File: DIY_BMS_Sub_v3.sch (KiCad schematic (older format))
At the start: 35 parts, among them J1 Conn_01x11, J2 Conn_02x04_Top_Bottom, J3 Conn_02x03_Top_Bottom, J4 Conn_02x03_Top_Bottom, SW1 SW_DIP_x04, U1 BQ76PL536A

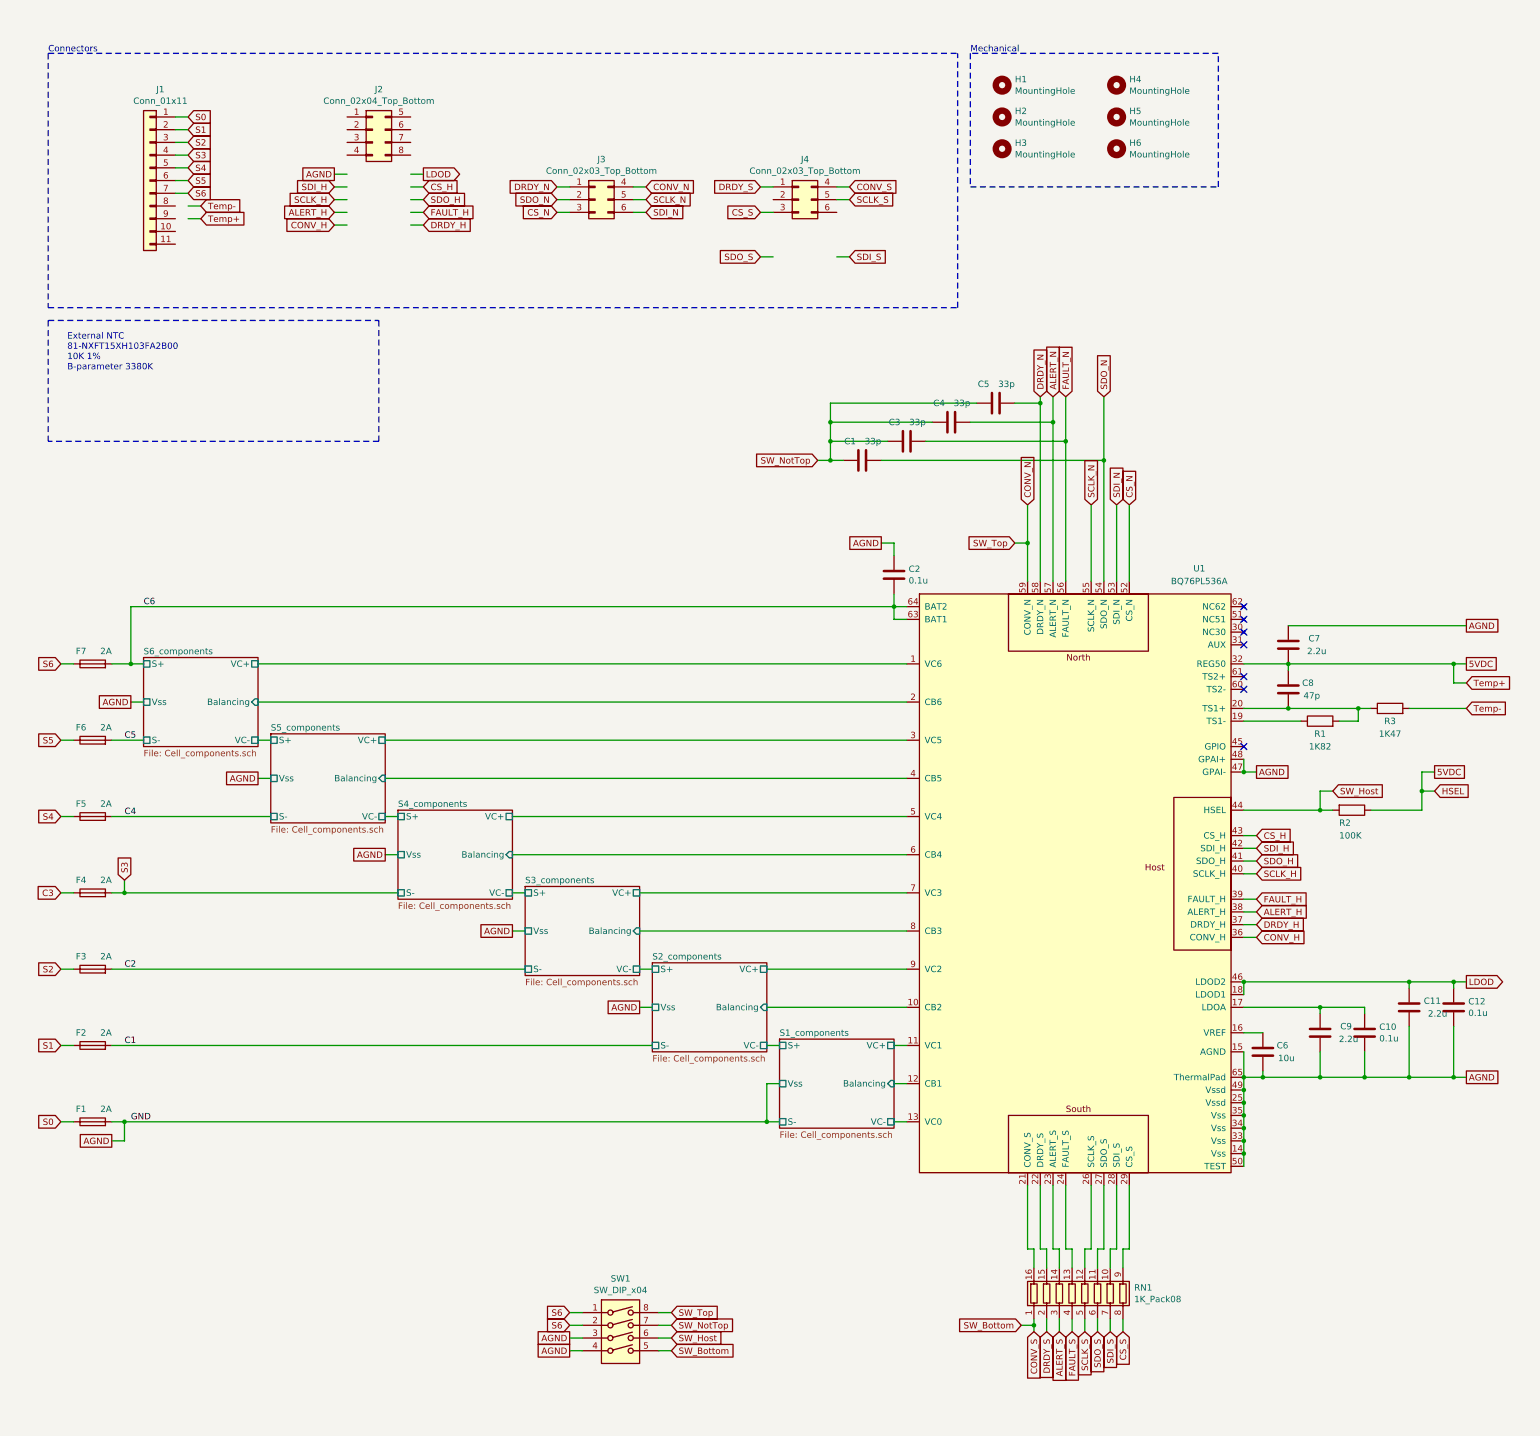
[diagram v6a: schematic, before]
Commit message: Add files via upload
Placed most components. Started routing and placing vias.
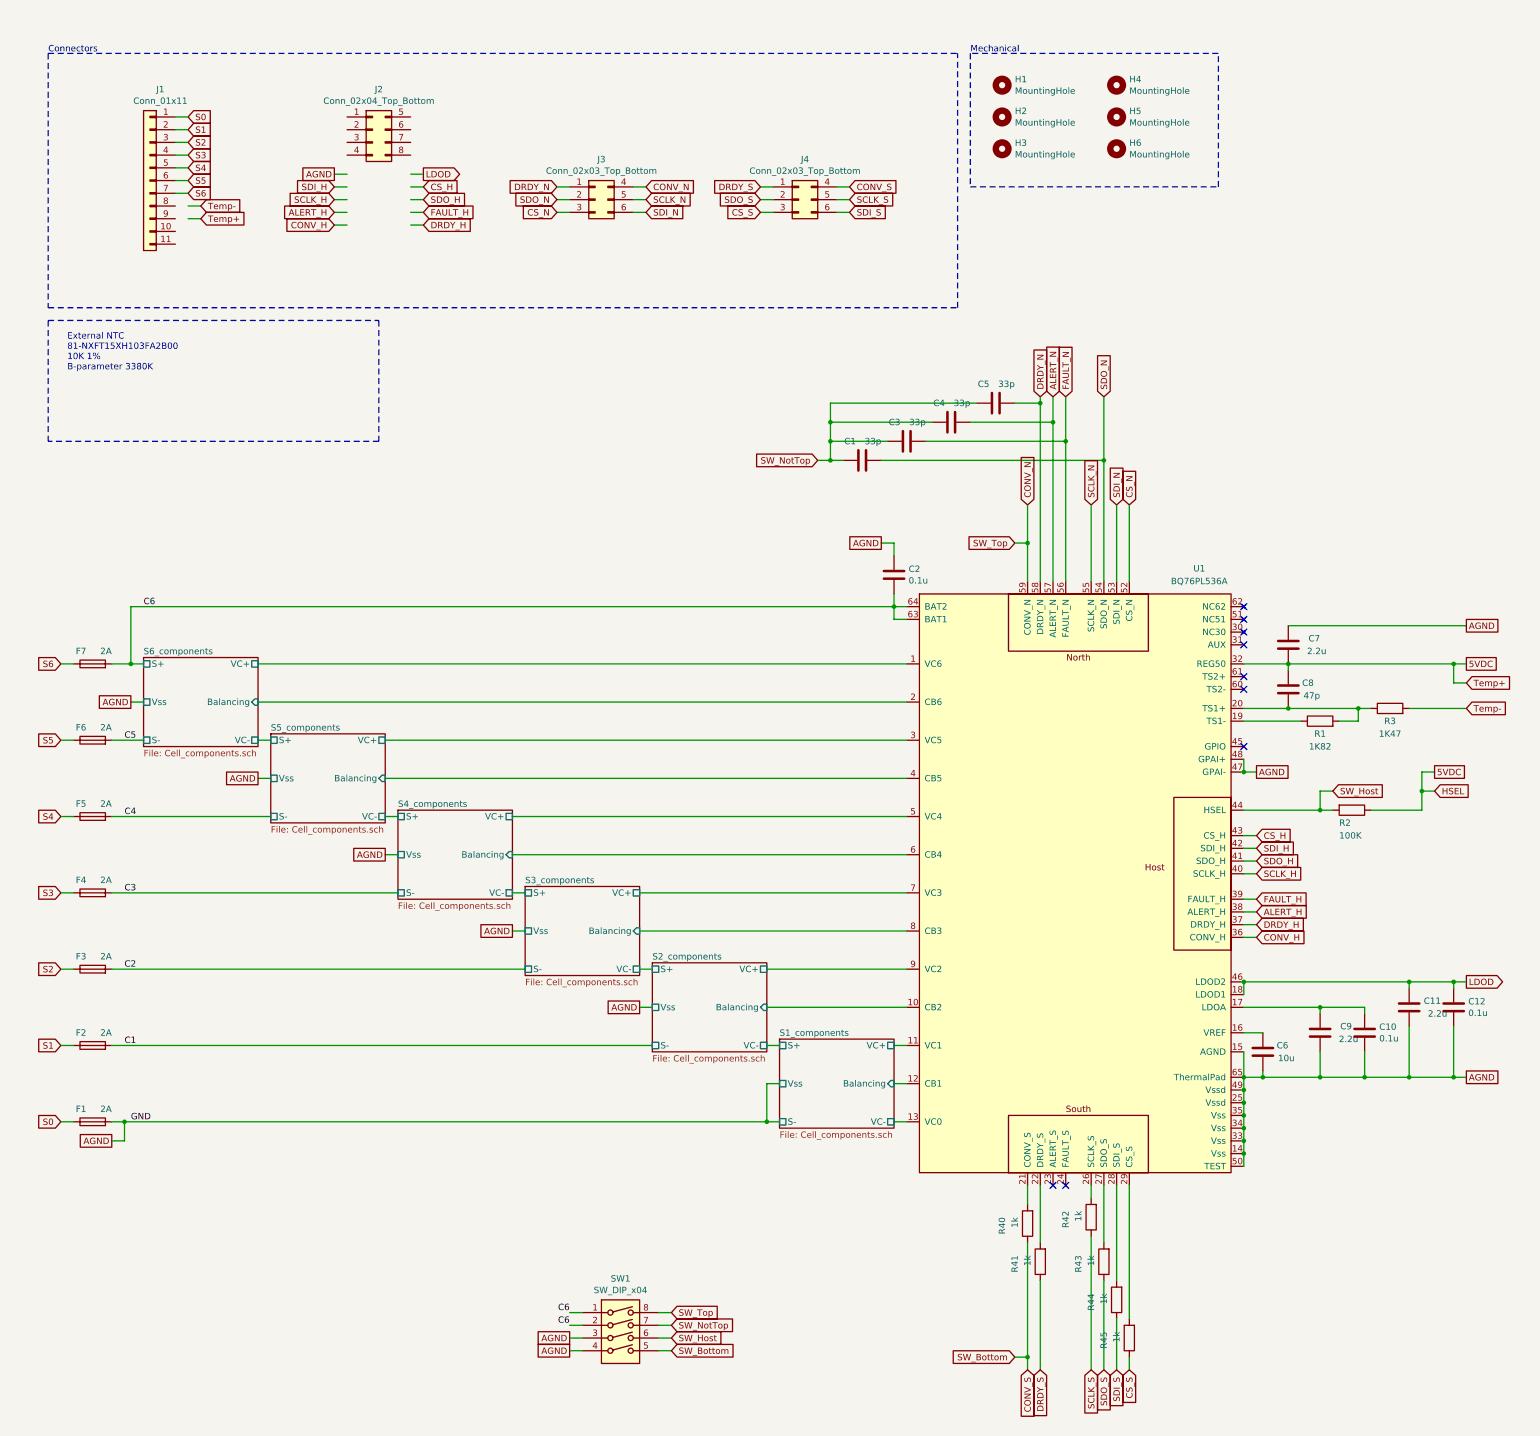
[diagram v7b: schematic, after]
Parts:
- removed RN1: 1K_Pack08, Resistor_SMD:R_Array_Convex_8x0602, symbol Device:R_Pack08
- added R40, R41, R42, R43, R44, R45: 1k, Resistor_SMD:R_0603_1608Metric_Pad1.05x0.95mm_HandSolder, symbol Device:R
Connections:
- net labels removed: ALERT_S, FAULT_S
- wire segments 216 -> 194
- no-connect marks 7 -> 9
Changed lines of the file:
@@
 S2
 Text GLabel 950  7450 0    50   Input ~ 0
-C3
+S3
 Text GLabel 950  6850 0    50   Input ~ 0
 S4
@@
 	0    -1   -1   0
 $EndComp
-$Comp
-L Device:R_Pack08 RN1
-U 1 1 5FBA3149
-P 9000 10600
-F 0 "RN1" H 9388 10646 50  0000 L CNN
-F 1 "1K_Pack08" H 9388 10555 50  0000 L CNN
-F 2 "Resistor_SMD:R_Array_Convex_8x0602" V 9475 10600 50  0001 C CNN
-F 3 "file:///C:/Users/HenkHenk/Downloads/AOC0000C14-1108062%20(2).pdf" H 9000 10600 50  0001 C CNN
-F 4 "667-EXB-2HV102JV" H 9000 10600 50  0001 C CNN "DPN"
-	1    9000 10600
-	1    0    0    -1
-$EndComp
-Wire Wire Line
-	9300 10250 9300 10400
-Wire Wire Line
-	8600 10250 8600 10400
-Wire Wire Line
-	8600 10250 8550 10250
-Wire Wire Line
-	8650 10250 8700 10250
-Wire Wire Line
-	8700 10250 8700 10400
-Wire Wire Line
-	8750 10250 8800 10250
-Wire Wire Line
-	8800 10250 8800 10400
-Wire Wire Line
-	8900 10400 8900 10250
-Wire Wire Line
-	8900 10250 8850 10250
-Wire Wire Line
-	9000 10400 9000 10250
-Wire Wire Line
-	9000 10250 9050 10250
-Wire Wire Line
-	9100 10400 9100 10250
-Wire Wire Line
-	9100 10250 9150 10250
-Wire Wire Line
-	8850 10250 8850 9750
-Wire Wire Line
-	8750 10250 8750 9750
-Wire Wire Line
-	9050 10250 9050 9750
-Wire Wire Line
-	9150 10250 9150 9750
-Wire Wire Line
-	9200 10400 9200 10250
-Wire Wire Line
-	9200 10250 9250 10250
-Wire Wire Line
-	9250 10250 9250 9750
-Wire Wire Line
-	9300 10250 9350 10250
-Wire Wire Line
-	8600 10800 8600 10850
-Wire Wire Line
-	8700 10800 8700 10900
-Wire Wire Line
-	8800 10800 8800 10900
-Wire Wire Line
-	8900 10800 8900 10900
-Wire Wire Line
-	9000 10800 9000 10900
-Wire Wire Line
-	9100 10800 9100 10900
-Wire Wire Line
-	9200 10800 9200 10900
-Wire Wire Line
-	9300 10800 9300 10900
 Text GLabel 4950 11050 0    50   UnSpc ~ 0
 AGND
-Wire Wire Line
-	9350 10250 9350 9750
-Wire Wire Line
-	8650 10250 8650 9750
-Text GLabel 9300 10900 3    50   Input ~ 0
-CS_S
 Text GLabel 6450 2100 0    50   Input ~ 0
 CS_S
 Wire Wire Line
 	6450 2100 6550 2100
-Text GLabel 9200 10900 3    50   Input ~ 0
+Text GLabel 7150 2100 2    50   Input ~ 0
 SDI_S
-Text GLabel 7150 2450 2    50   Input ~ 0
-SDI_S
-Wire Wire Line
-	7150 2450 7050 2450
-Text GLabel 9100 10900 3    50   Input ~ 0
+Wire Wire Line
+	7150 2100 7050 2100
+Text GLabel 6450 2000 0    50   Input ~ 0
 SDO_S
-Text GLabel 6450 2450 0    50   Input ~ 0
-SDO_S
-Wire Wire Line
-	6450 2450 6550 2450
-Text GLabel 9000 10900 3    50   Input ~ 0
-SCLK_S
-Text GLabel 8600 10900 3    50   Input ~ 0
-CONV_S
+Wire Wire Line
+	6450 2000 6550 2000
 Text GLabel 7150 1900 2    50   Input ~ 0
 CONV_S
 Wire Wire Line
 	7150 1900 7050 1900
-Text GLabel 8700 10900 3    50   Input ~ 0
-DRDY_S
 Text GLabel 6450 1900 0    50   Input ~ 0
 DRDY_S
 Wire Wire Line
 	6450 1900 6550 1900
-Text GLabel 8800 10900 3    50   Input ~ 0
-ALERT_S
-Text GLabel 8900 10900 3    50   Input ~ 0
-FAULT_S
 NoConn ~ 10250 5500
 NoConn ~ 10250 5200
@@
 Wire Wire Line
 	4950 11050 5050 11050
-Text GLabel 8500 10850 0    50   Input ~ 0
-SW_Bottom
-Wire Wire Line
-	8500 10850 8600 10850
 Wire Wire Line
 	5050 10950 4950 10950
@@
 Wire Wire Line
 	10850 6800 10950 6800
-Text GLabel 4950 10850 0    50   Input ~ 0
-S6
 Text GLabel 8450 4700 0    50   Input ~ 0
 SW_Top
@@
 Wire Wire Line
 	5050 10750 4950 10750
-Text GLabel 4950 10750 0    50   Input ~ 0
-S6
 Text GLabel 6900 4050 0    50   Input ~ 0
 SW_NotTop
@@
 	6900 4050 7000 4050
 Connection ~ 7000 4050
-Connection ~ 8600 10850
-Wire Wire Line
-	8600 10850 8600 10900
-Wire Wire Line
-	8550 9750 8550 10250
 Text GLabel 12000 8150 2    50   Output ~ 0
 LDOD
@@
 	4600 8050 1350 8050
 Wire Wire Line
-	1350 7450 1450 7450
-Wire Wire Line
 	1350 6850 2600 6850
 Wire Wire Line
@@
 Text Label 1450 6250 0    50   ~ 0
 C5
-Text GLabel 1450 7350 1    50   Input ~ 0
-S3
-Wire Wire Line
-	1450 7350 1450 7450
-Connection ~ 1450 7450
-Wire Wire Line
-	1450 7450 3600 7450
 $Comp
 L Connector_Generic:Conn_02x03_Top_Bottom J3
@@
 Text GLabel 1950 1350 2    50   Input ~ 0
 S0
+Wire Wire Line
+	1350 7450 3600 7450
+Text Label 1450 7450 0    50   ~ 0
+C3
+NoConn ~ 8750 9750
+NoConn ~ 8850 9750
+$Comp
+L Device:R R?
+U 1 1 612B0B90
+P 8650 10350
+AR Path="/5FAF2B15/612B0B90" Ref="R?"  Part="1"
+AR Path="/5FB201DB/612B0B90" Ref="R?"  Part="1"
+AR Path="/5FB24C66/612B0B90" Ref="R?"  Part="1"
+AR Path="/5FA9BBC5/612B0B90" Ref="R?"  Part="1"
+AR Path="/5FA9D4E1/612B0B90" Ref="R?"  Part="1"
+AR Path="/5FAA7870/612B0B90" Ref="R?"  Part="1"
+AR Path="/612B0B90" Ref="R41"  Part="1"
+F 0 "R41" V 8850 10300 50  0000 L CNN
+F 1 "1k" V 8750 10300 50  0000 L CNN
+F 2 "Resistor_SMD:R_0603_1608Metric_Pad1.05x0.95mm_HandSolder" V 8580 10350 50  0001 C CNN
+F 3 "~" H 8650 10350 50  0001 C CNN
+F 4 "C21190" V 8650 10350 50  0001 C CNN "LCSC"
+	1    8650 10350
+	-1   0    0    1
+$EndComp
+$Comp
+L Device:R R?
+U 1 1 612BC744
+P 9050 10000
+AR Path="/5FAF2B15/612BC744" Ref="R?"  Part="1"
+AR Path="/5FB201DB/612BC744" Ref="R?"  Part="1"
+AR Path="/5FB24C66/612BC744" Ref="R?"  Part="1"
+AR Path="/5FA9BBC5/612BC744" Ref="R?"  Part="1"
+AR Path="/5FA9D4E1/612BC744" Ref="R?"  Part="1"
+AR Path="/5FAA7870/612BC744" Ref="R?"  Part="1"
+AR Path="/612BC744" Ref="R42"  Part="1"
+F 0 "R42" V 9250 9950 50  0000 L CNN
+F 1 "1k" V 9150 9950 50  0000 L CNN
+F 2 "Resistor_SMD:R_0603_1608Metric_Pad1.05x0.95mm_HandSolder" V 8980 10000 50  0001 C CNN
+F 3 "~" H 9050 10000 50  0001 C CNN
+F 4 "C21190" V 9050 10000 50  0001 C CNN "LCSC"
+	1    9050 10000
+	-1   0    0    1
+$EndComp
+$Comp
+L Device:R R?
+U 1 1 612C873E
+P 9150 10350
+AR Path="/5FAF2B15/612C873E" Ref="R?"  Part="1"
+AR Path="/5FB201DB/612C873E" Ref="R?"  Part="1"
+AR Path="/5FB24C66/612C873E" Ref="R?"  Part="1"
+AR Path="/5FA9BBC5/612C873E" Ref="R?"  Part="1"
+AR Path="/5FA9D4E1/612C873E" Ref="R?"  Part="1"
+AR Path="/5FAA7870/612C873E" Ref="R?"  Part="1"
+AR Path="/612C873E" Ref="R43"  Part="1"
+F 0 "R43" V 9350 10300 50  0000 L CNN
+F 1 "1k" V 9250 10300 50  0000 L CNN
+F 2 "Resistor_SMD:R_0603_1608Metric_Pad1.05x0.95mm_HandSolder" V 9080 10350 50  0001 C CNN
+F 3 "~" H 9150 10350 50  0001 C CNN
+F 4 "C21190" V 9150 10350 50  0001 C CNN "LCSC"
+	1    9150 10350
+	-1   0    0    1
+$EndComp
+$Comp
+L Device:R R?
+U 1 1 612D482A
+P 9250 10650
+AR Path="/5FAF2B15/612D482A" Ref="R?"  Part="1"
+AR Path="/5FB201DB/612D482A" Ref="R?"  Part="1"
+AR Path="/5FB24C66/612D482A" Ref="R?"  Part="1"
+AR Path="/5FA9BBC5/612D482A" Ref="R?"  Part="1"
+AR Path="/5FA9D4E1/612D482A" Ref="R?"  Part="1"
+AR Path="/5FAA7870/612D482A" Ref="R?"  Part="1"
+AR Path="/612D482A" Ref="R44"  Part="1"
+F 0 "R44" V 9450 10600 50  0000 L CNN
+F 1 "1k" V 9350 10600 50  0000 L CNN
+F 2 "Resistor_SMD:R_0603_1608Metric_Pad1.05x0.95mm_HandSolder" V 9180 10650 50  0001 C CNN
+F 3 "~" H 9250 10650 50  0001 C CNN
+F 4 "C21190" V 9250 10650 50  0001 C CNN "LCSC"
+	1    9250 10650
+	-1   0    0    1
+$EndComp
+$Comp
+L Device:R R?
+U 1 1 612EC730
+P 9350 10950
+AR Path="/5FAF2B15/612EC730" Ref="R?"  Part="1"
+AR Path="/5FB201DB/612EC730" Ref="R?"  Part="1"
+AR Path="/5FB24C66/612EC730" Ref="R?"  Part="1"
+AR Path="/5FA9BBC5/612EC730" Ref="R?"  Part="1"
+AR Path="/5FA9D4E1/612EC730" Ref="R?"  Part="1"
+AR Path="/5FAA7870/612EC730" Ref="R?"  Part="1"
+AR Path="/612EC730" Ref="R45"  Part="1"
+F 0 "R45" V 9550 10900 50  0000 L CNN
+F 1 "1k" V 9450 10900 50  0000 L CNN
+F 2 "Resistor_SMD:R_0603_1608Metric_Pad1.05x0.95mm_HandSolder" V 9280 10950 50  0001 C CNN
+F 3 "~" H 9350 10950 50  0001 C CNN
+F 4 "C21190" V 9350 10950 50  0001 C CNN "LCSC"
+	1    9350 10950
+	-1   0    0    1
+$EndComp
+Wire Wire Line
+	9350 10800 9350 9750
+Wire Wire Line
+	9250 10500 9250 9750
+Wire Wire Line
+	9150 9750 9150 10200
+Wire Wire Line
+	9050 9750 9050 9850
+Wire Wire Line
+	8550 9900 8550 9750
+Wire Wire Line
+	8650 9750 8650 10200
+Connection ~ 8550 11100
+Wire Wire Line
+	8450 11100 8550 11100
+Text GLabel 8450 11100 0    50   Input ~ 0
+SW_Bottom
+Text GLabel 8650 11200 3    50   Input ~ 0
+DRDY_S
+Text GLabel 8550 11200 3    50   Input ~ 0
+CONV_S
+Text GLabel 9350 11200 3    50   Input ~ 0
+CS_S
+Wire Wire Line
+	9350 11100 9350 11200
+Text GLabel 9250 11200 3    50   Input ~ 0
+SDI_S
+Text GLabel 9150 11200 3    50   Input ~ 0
+SDO_S
+Text GLabel 9050 11200 3    50   Input ~ 0
+SCLK_S
+Wire Wire Line
+	8550 10200 8550 11100
+Wire Wire Line
+	9050 10150 9050 11200
+Wire Wire Line
+	9150 10500 9150 11200
+Wire Wire Line
+	9250 10800 9250 11200
+$Comp
+L Device:R R?
+U 1 1 6127E907
+P 8550 10050
+AR Path="/5FAF2B15/6127E907" Ref="R?"  Part="1"
+AR Path="/5FB201DB/6127E907" Ref="R?"  Part="1"
+AR Path="/5FB24C66/6127E907" Ref="R?"  Part="1"
+AR Path="/5FA9BBC5/6127E907" Ref="R?"  Part="1"
+AR Path="/5FA9D4E1/6127E907" Ref="R?"  Part="1"
+AR Path="/5FAA7870/6127E907" Ref="R?"  Part="1"
+AR Path="/6127E907" Ref="R40"  Part="1"
+F 0 "R40" V 8750 10000 50  0000 L CNN
+F 1 "1k" V 8650 10000 50  0000 L CNN
+F 2 "Resistor_SMD:R_0603_1608Metric_Pad1.05x0.95mm_HandSolder" V 8480 10050 50  0001 C CNN
+F 3 "~" H 8550 10050 50  0001 C CNN
+F 4 "C21190" V 8550 10050 50  0001 C CNN "LCSC"
+	1    8550 10050
+	-1   0    0    1
+$EndComp
+Wire Wire Line
+	8550 11100 8550 11200
+Wire Wire Line
+	8650 10500 8650 11200
+Text Label 4950 10750 2    50   ~ 0
+C6
+Text Label 4950 10850 2    50   ~ 0
+C6
 $EndSCHEMATC
